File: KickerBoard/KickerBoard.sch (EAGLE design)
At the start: 113 parts, among them J1 53375-0610, Q1 TK12P60W, Q4 BSS138, Q5 BSP130, Q6 ZXTN08400BFF, U1 LPC1549JBD48, U10 AD8601, U11 ADCMP350YKSZ, U2 LM5160QPWPRQ1, U3 UCC27212DPRT, U4 UCC27512DRSR, U5 IC-AD_ADR5041, U6 MCP1700T-33, U7 LT6108-2, U8 UCC27524DGN-NOPAD, U9 INA213

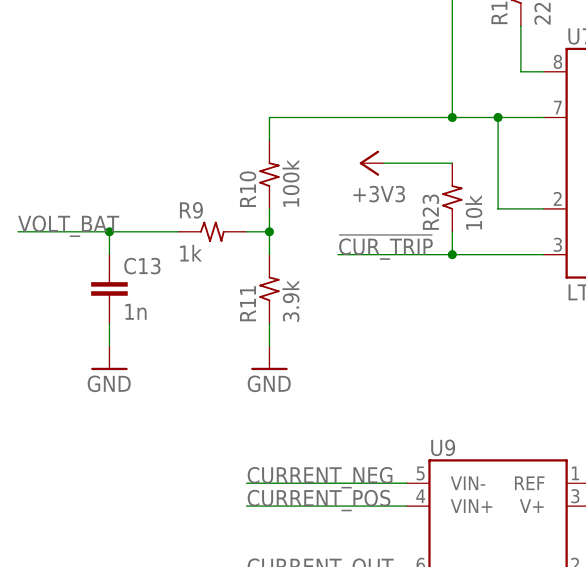
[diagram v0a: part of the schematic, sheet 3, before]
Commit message: 電源監視部分のLPF遮断周波数を下げた
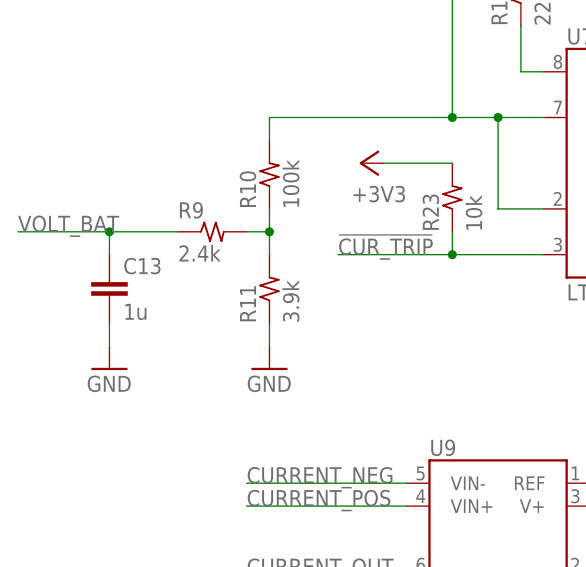
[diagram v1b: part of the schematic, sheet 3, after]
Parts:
- C13: value 1n -> 1u
- R9: value 1k -> 2.4k
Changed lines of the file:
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@@
 <part name="+3V2" library="MotorDriver" deviceset="+3V3" device=""/>
 <part name="U7" library="ic-LT" deviceset="LT6108-2" device=""/>
-<part name="C13" library="Passive" deviceset="C" device="1608" value="1n"/>
-<part name="R9" library="Passive" deviceset="R" device="1608" value="1k"/>
+<part name="C13" library="Passive" deviceset="C" device="1608" value="1u"/>
+<part name="R9" library="Passive" deviceset="R" device="1608" value="2.4k"/>
 <part name="R10" library="Passive" deviceset="R" device="1608" value="100k"/>
 <part name="R11" library="Passive" deviceset="R" device="1608" value="3.9k"/>

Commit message: KickerBoardの部品表作成(途中)
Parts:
- added C1: 0.33n, Passive:C1608
- added R50: 10k, Passive:R1608
- C10, C9: value 2.2u -> 0.1u
- C11, C12, C3: value 1u -> 0.1u
- C13: value 1u -> 0.22u
- C17: value (none) -> 0.1u
- C5: value 47u -> 22u
- C6, C7: value 22u -> 0.22u
- C8: value 10u -> 4.7u; device Passive:C1608 -> Passive:C3216
- D9: value (none) -> RB520S
- R11: value 3.9k -> 4.7k
- R29, R31: value 10k -> 33k
- R30: value 1k -> 2.2k
- R4: value 10 -> 100
- R45, R46, R47: value (none) -> 100
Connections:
- net GND: now also C1.2, R50.1
- net N$20: now also R50.2
- net VOLT_CUR: now also C1.1
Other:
- note added: "ASPIAIG-S6055-470M-T"
- note added: "Av=16 (1+33k/2.2k)"
- note added: "Vc_max=235[V]"
- note added: "Vout=1.597[V]@Vcap=150[V]"
- note added: "Vout=2.129[V]@Vcap=200[V]"
- note added: "Vout=2.448[V]@Vcap=230[V]"
- note added: "fc=168.5[kHz]"
- note added: "fc=301[Hz]"
- note removed: "Av=11 (1+10k/1k)"
- note removed: "SRN6045TA-470MCT-ND"
- note removed: "Vout=1.098[V]@Vcap=150[V]"
- note removed: "Vout=1.464[V]@Vcap=200[V]"
- note removed: "Vout=1.683[V]@Vcap=230[V]"

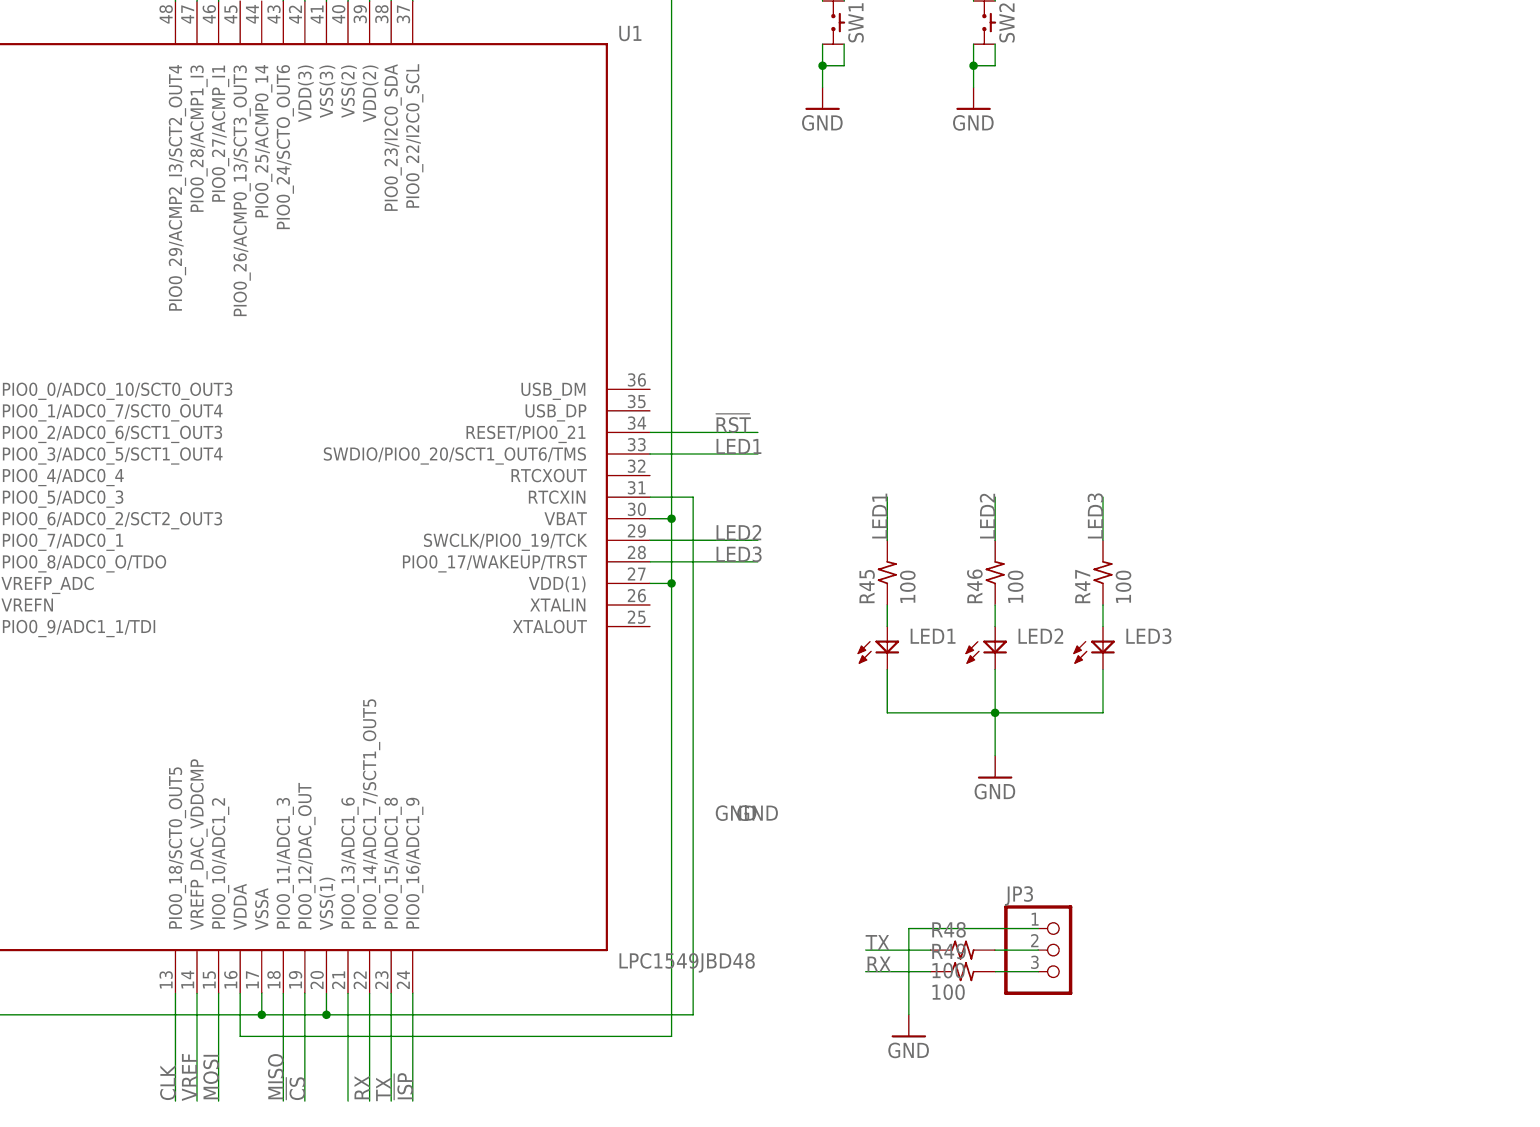
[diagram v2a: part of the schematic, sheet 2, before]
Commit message: メインとの通信をSPIからCANに切り替えた
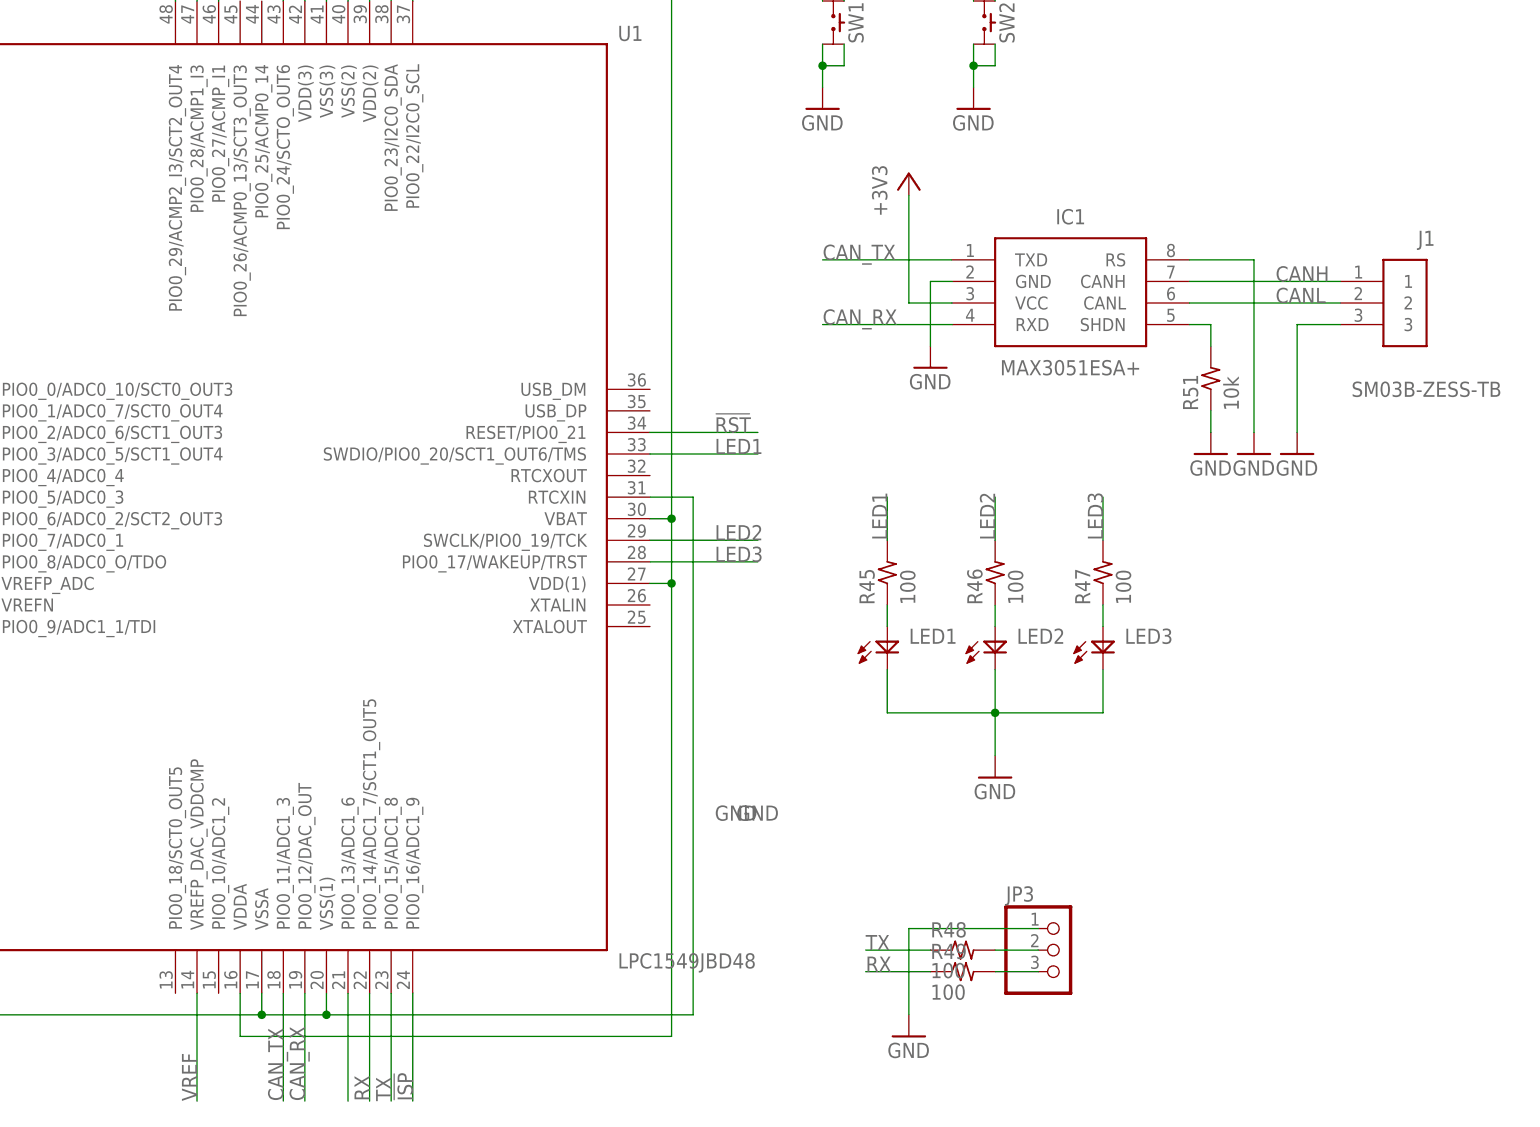
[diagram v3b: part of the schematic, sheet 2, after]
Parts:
- added IC1: MAX3051ESA+, MAX3051ESA+:MAX3051ESA+
- added R51: 10k, MotorDriver:R1005
- J1: value 53375-0610 -> SM03B-ZESS-TB; device MotorDriver:53375-0610 -> SM03B-ZESS-TB:SM03B-ZESS-TB
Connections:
- removed net !CS: J1.2, U1.PIO0_12/DAC_OUT
- removed net CLK: J1.5, U1.PIO0_18/SCT0_OUT5
- removed net MISO: J1.3, U1.PIO0_11/ADC1_3
- removed net MOSI: J1.4, U1.PIO0_10/ADC1_2
- new net CANH: IC1.CANH, J1.1
- new net CANL: IC1.CANL, J1.2
- new net CAN_RX: IC1.RXD, U1.PIO0_12/DAC_OUT
- new net CAN_TX: IC1.TXD, U1.PIO0_11/ADC1_3
- new net N$34: IC1.SHDN, R51.2
- net +3V3: now also IC1.VCC
- net +5V: no longer J1.1
- net GND: now also IC1.GND, IC1.RS, J1.3, R51.1; no longer J1.6

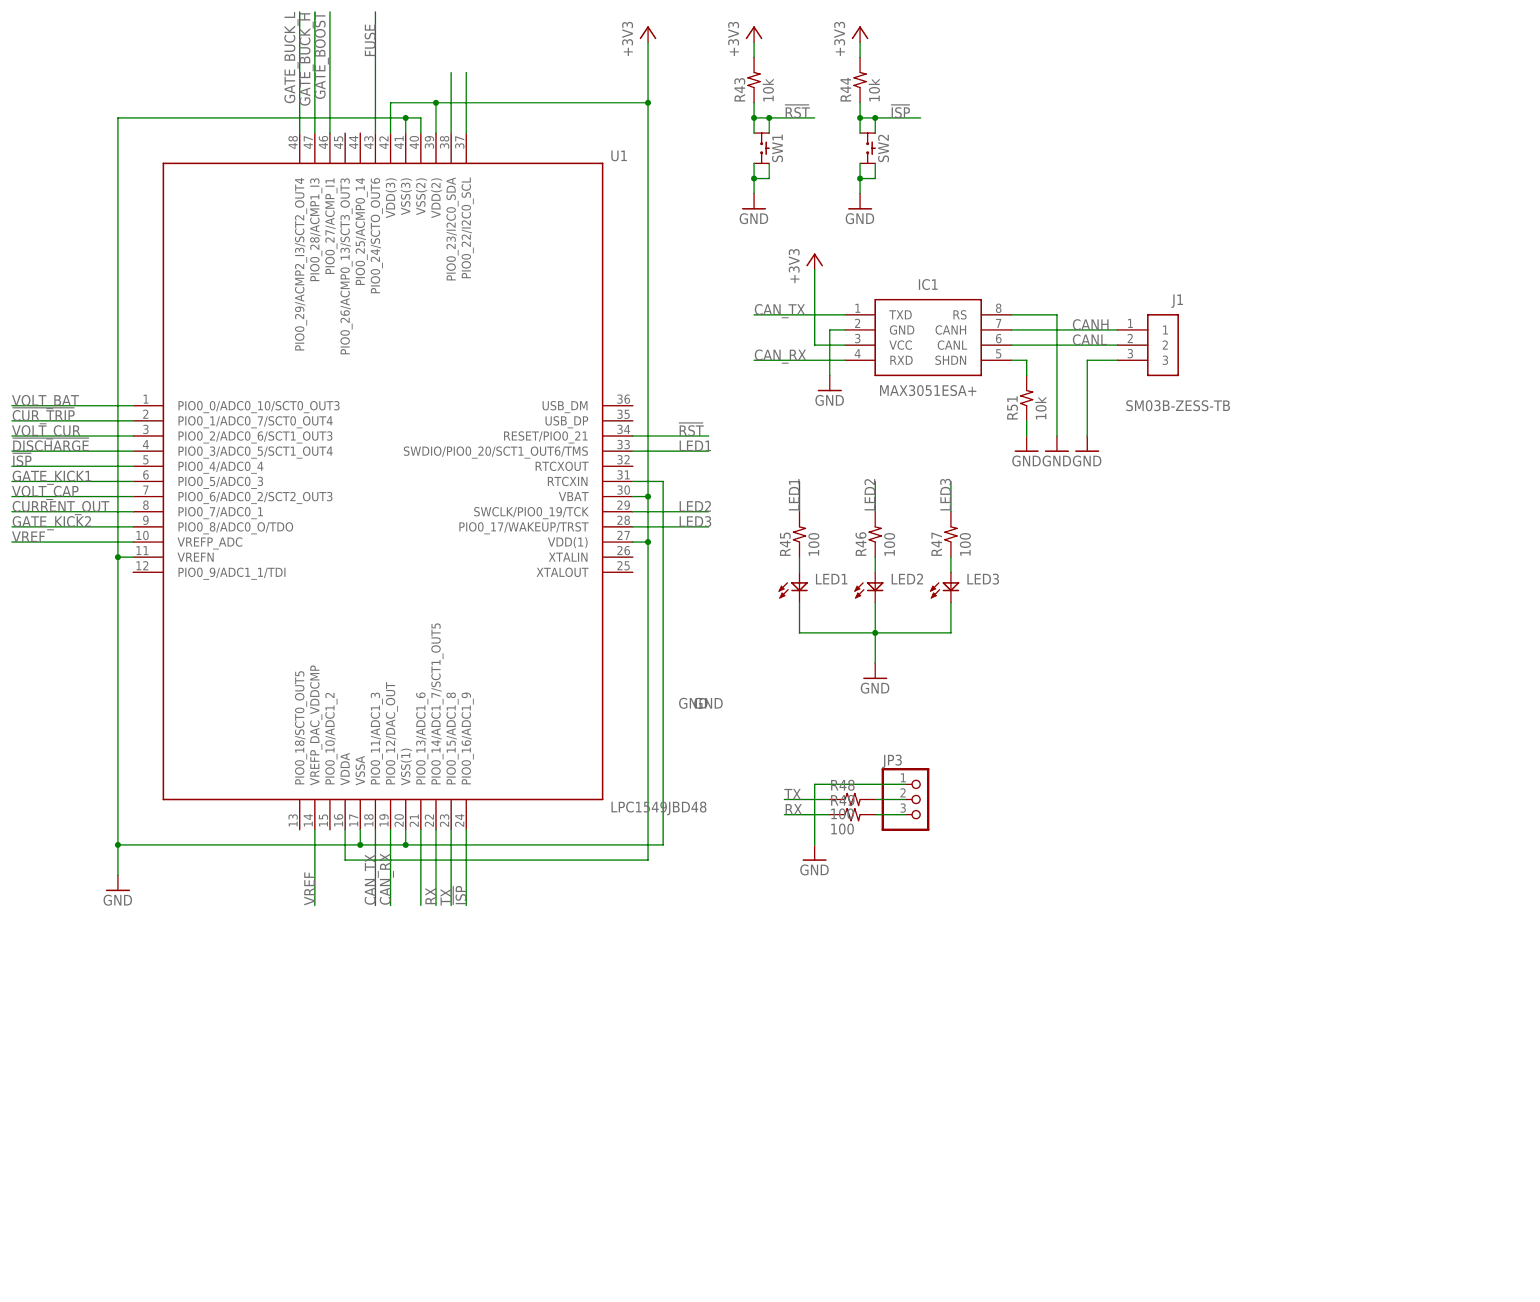
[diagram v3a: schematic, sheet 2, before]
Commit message: 書き込み部・電源部を変更
*書き込みをUARTからUSBに変更
  *USBコネクタを追加
  *12[MHz]クロックを追加
  *保護ICを追加
  *ピンヘッダを削除
*5[V]電源の削除
  *5[V]を使用している箇所がなかったので無くした
  *レギュレータを5[V]->3.3[V]から12[V]->3.3[V]に
  *USBのVBUSはレギュレータのみに入る
  *VBUS, 12[V]へ逆流防止ダイオードを追加
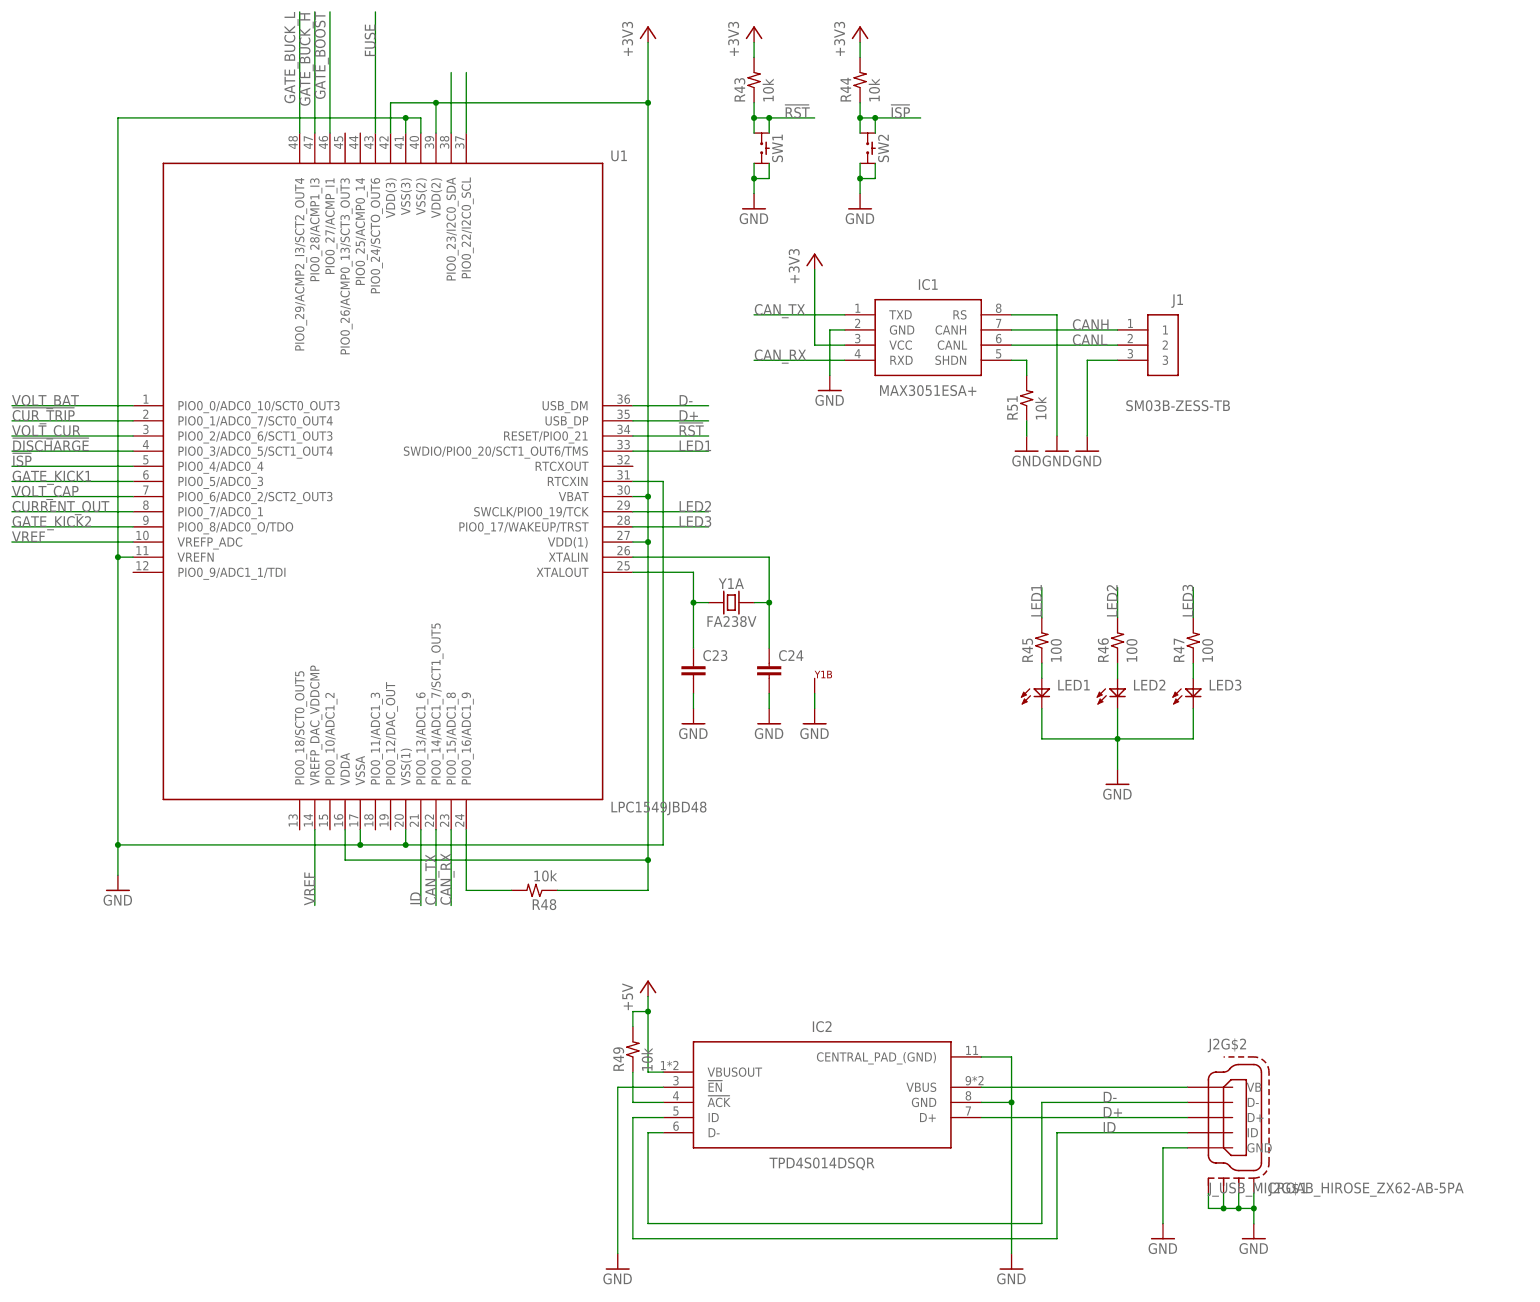
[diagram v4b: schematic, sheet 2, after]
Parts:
- removed JP3: (no value), MotorDriver:HEADER-1X3ROUND
- removed U6: MCP1700T-33, MotorDriver:MCP1700T-33
- added C22: 470p, Passive:C1608
- added C23, C24: (no value), MotorDriver:C1608
- added D11: SDM2U40CSP-7B, SDM2U40CSP-7B:SDM2U40CSP-7B
- added IC2: TPD4S014DSQR, TPD4S014DSQR:TPD4S014DSQR
- added J2: J_USB_MICROAB_HIROSE_ZX62-AB-5PA, j_usb_hirose_zx62-ab-5pa:J_USB_MICROAB_HIROSE_ZX62-AB-5PA
- added U12: MIC5219-3.3YMM, MIC5219-3.3YMM:MIC5219-3.3YMM
- added Y1: FA238V, FA238V:FA238V
- D2: value (none) -> SDM2U40CSP-7B; device Diode:SBD-SOD523 -> SDM2U40CSP-7B:SDM2U40CSP-7B
- R48, R49: value 100 -> 10k; device MotorDriver:R1608 -> MotorDriver:R1005
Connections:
- removed net N$52: JP3.3, R49.2
- removed net RX: R49.1, U1.PIO0_14/ADC1_7/SCT1_OUT5
- removed net TX: R48.1, U1.PIO0_15/ADC1_8
- new net D+: IC2.D+, J2G$2.D+, U1.USB_DP
- new net D-: IC2.D-, J2G$2.D-, U1.USB_DM
- new net ID: IC2.ID, J2G$2.ID, U1.PIO0_13/ADC1_6
- new net N$40: C11.1, D11.K, D2.K, U12.EN, U12.IN
- new net N$50: R48.2, U1.PIO0_16/ADC1_9
- new net N$51: IC2.!ACK, R49.1
- new net N$54: C22.1, U12.BYP
- new net N$56: IC2.VBUS, J2G$2.VB
- net !ISP: no longer U1.PIO0_16/ADC1_9
- net +12V: now also D2.A
- net +3V3: now also R48.1, U12.OUT; no longer D2.A, U6.VO
- net +5V: now also D11.A, IC2.VBUSOUT, R49.2; no longer C11.1, D2.K, U6.VI
- net CAN_RX: now also U1.PIO0_15/ADC1_8; no longer U1.PIO0_12/DAC_OUT
- net CAN_TX: now also U1.PIO0_14/ADC1_7/SCT1_OUT5; no longer U1.PIO0_11/ADC1_3
- net GND: now also C22.2, C23.2, C24.2, IC2.!EN, IC2.CENTRAL_PAD_(GND), IC2.GND, J2G$1.S1, J2G$1.S2, J2G$1.S3, J2G$1.S4, J2G$2.GND, U12.GND, Y1B.1; no longer JP3.1, U6.GND
- net N$47: now also C24.1, U1.XTALIN, Y1A.3; no longer U1.PIO0_13/ADC1_6
- net N$48: now also C23.1, U1.XTALOUT, Y1A.1; no longer JP3.2, R48.2
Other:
- moved on the sheet: C11, C12, LED1, LED2, LED3, R45, R46, R47, R48, R49, R8, U5

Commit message: viaの数とかを調節した
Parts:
- added R52, R53: 2.2, MotorDriver:R1608
- R19: value 10 -> 2.2; device Passive:R2012 -> MotorDriver:R1608
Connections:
- new net N$52: R52.2, U$1.G
- new net N$53: R53.2, U$2.G
- net GND: no longer R50.1
- net N$19: now also R53.1; no longer U$2.G
- net N$20: now also R52.1; no longer U$1.G
- net N$21: now also R50.1
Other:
- moved on the sheet: C15, C21, D3, D4, L2, Q1, R15, R16, R19, R20, R50, U$1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
